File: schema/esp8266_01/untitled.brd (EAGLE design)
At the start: 40.3 x 53.3 mm, 15 parts, among them IC1 LD117AS33TR, X1 22-23-2021

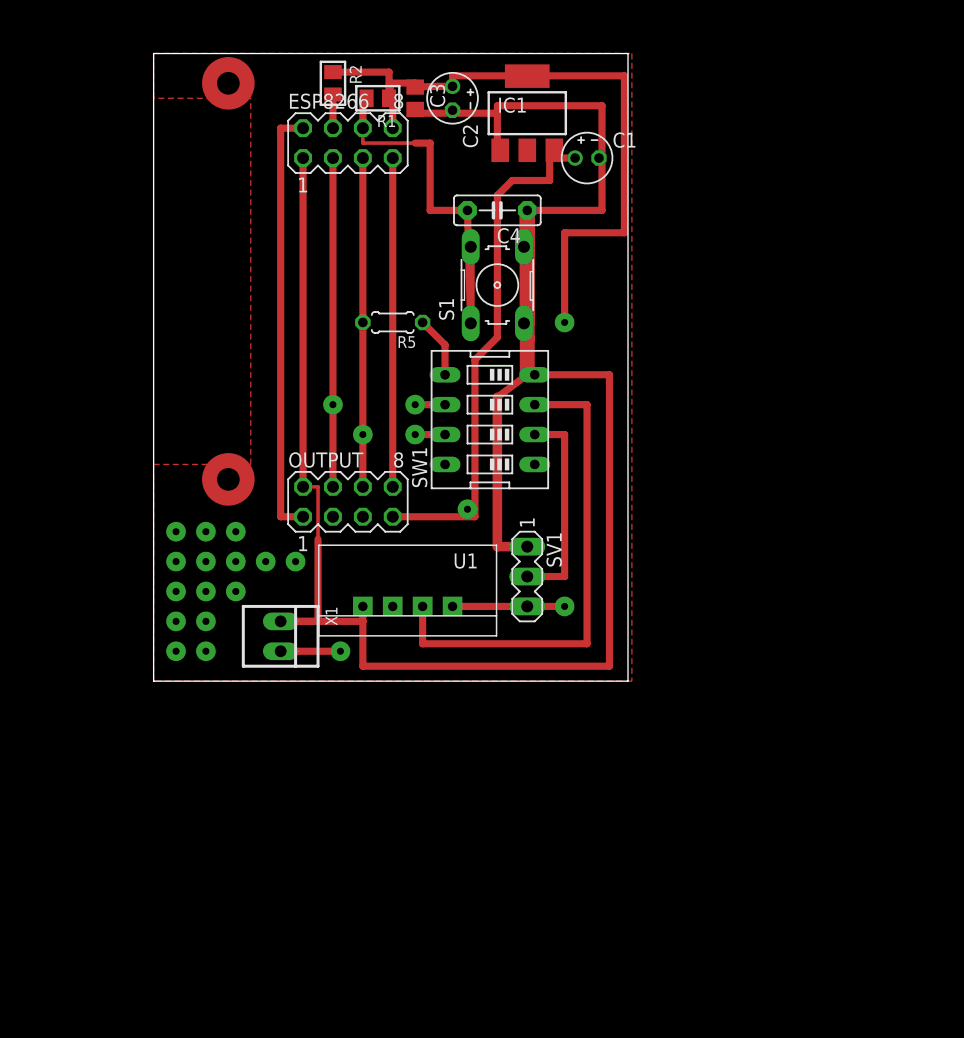
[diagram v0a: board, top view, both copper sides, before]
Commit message: Added ch340
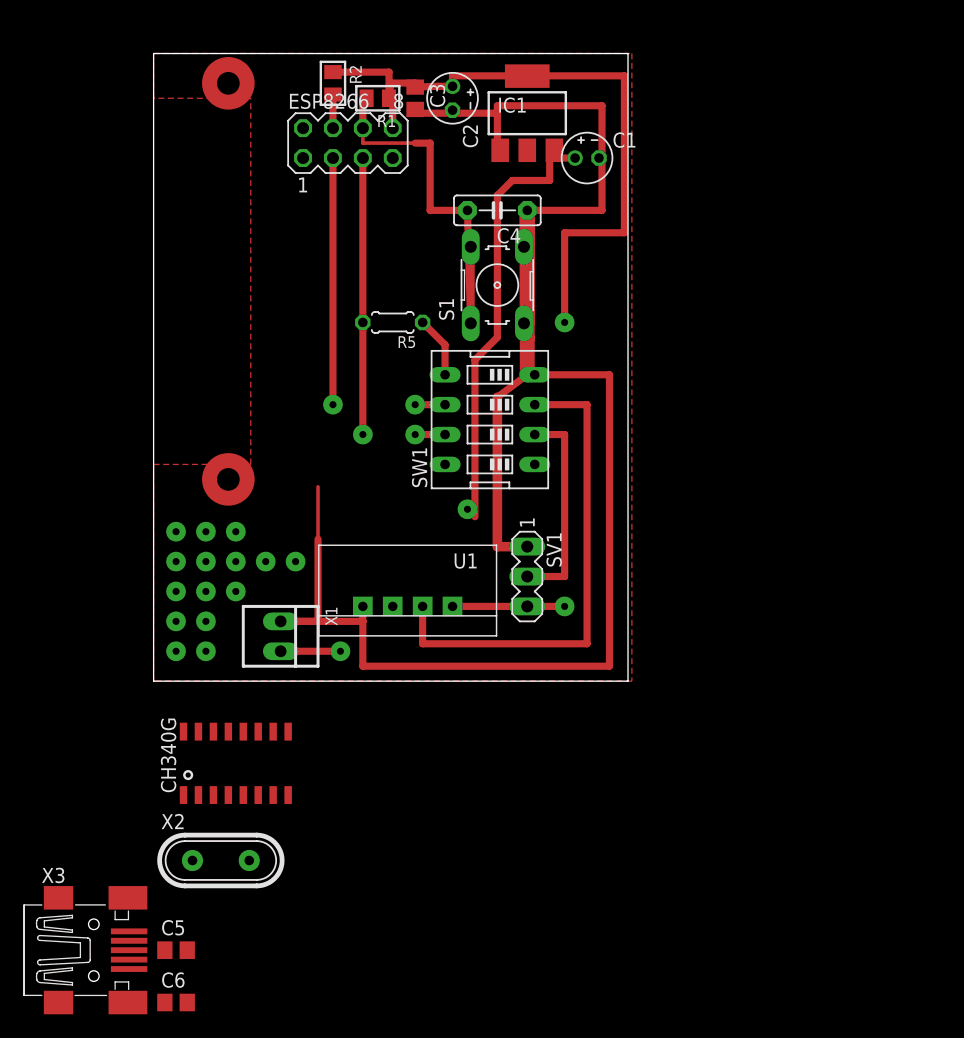
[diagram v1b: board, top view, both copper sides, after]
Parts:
- removed OUTPUT: (no value), con-lstb:MA04-2
- added C5, C6: 22 pF, rcl:C0805
- added U$1: CH340G, usb-serial:SOIC16
- added X2: 12 MHz, IQD-Frequency-Products:HC49
- added X3: MINI-USB-32005-301, con-cypressindustries:32005-301
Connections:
- new net N$27: C5.2, U$1.7, X2.1
- new net N$28: C6.2, U$1.8, X2.2
- net GND: now also C5.1, C6.1; no longer OUTPUT.2
- net GPIO0: no longer OUTPUT.6
- net GPIO2: no longer OUTPUT.4
- net N$11: now also X3.1; no longer OUTPUT.7
- net RX: now also U$1.2; no longer OUTPUT.8
- net TX: now also U$1.3; no longer OUTPUT.1
- net VCC: now also U$1.16
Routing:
- net TX: track 36.8 -> 0.00 mm
- net GND: track 215.7 -> 186.5 mm
- net RX: track 27.9 -> 0.00 mm
- net N$11: track 50.0 -> 43.0 mm
- net GPIO2: track 30.5 -> 23.5 mm
- net GPIO0: track 30.5 -> 26.0 mm
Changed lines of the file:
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@@
 <layers>
 <layer number="1" name="Top" color="4" fill="1" visible="yes" active="yes"/>
-<layer number="16" name="Bottom" color="1" fill="1" visible="no" active="yes"/>
+<layer number="16" name="Bottom" color="1" fill="1" visible="yes" active="yes"/>
 <layer number="17" name="Pads" color="2" fill="1" visible="yes" active="yes"/>
 <layer number="18" name="Vias" color="2" fill="1" visible="yes" active="yes"/>
-<layer number="19" name="Unrouted" color="6" fill="1" visible="no" active="yes"/>
-<layer number="20" name="Dimension" color="15" fill="1" visible="no" active="yes"/>
-<layer number="21" name="tPlace" color="7" fill="1" visible="no" active="yes"/>
-<layer number="22" name="bPlace" color="7" fill="1" visible="no" active="yes"/>
-<layer number="23" name="tOrigins" color="15" fill="1" visible="no" active="yes"/>
-<layer number="24" name="bOrigins" color="15" fill="1" visible="no" active="yes"/>
-<layer number="25" name="tNames" color="7" fill="1" visible="no" active="yes"/>
-<layer number="26" name="bNames" color="7" fill="1" visible="no" active="yes"/>
-<layer number="27" name="tValues" color="7" fill="1" visible="no" active="yes"/>
-<layer number="28" name="bValues" color="7" fill="1" visible="no" active="yes"/>
+<layer number="19" name="Unrouted" color="6" fill="1" visible="yes" active="yes"/>
+<layer number="20" name="Dimension" color="15" fill="1" visible="yes" active="yes"/>
+<layer number="21" name="tPlace" color="7" fill="1" visible="yes" active="yes"/>
+<layer number="22" name="bPlace" color="7" fill="1" visible="yes" active="yes"/>
+<layer number="23" name="tOrigins" color="15" fill="1" visible="yes" active="yes"/>
+<layer number="24" name="bOrigins" color="15" fill="1" visible="yes" active="yes"/>
+<layer number="25" name="tNames" color="7" fill="1" visible="yes" active="yes"/>
+<layer number="26" name="bNames" color="7" fill="1" visible="yes" active="yes"/>
+<layer number="27" name="tValues" color="7" fill="1" visible="yes" active="yes"/>
+<layer number="28" name="bValues" color="7" fill="1" visible="yes" active="yes"/>
 <layer number="29" name="tStop" color="7" fill="3" visible="no" active="yes"/>
 <layer number="30" name="bStop" color="7" fill="6" visible="no" active="yes"/>
@@
 </element>
 <element name="IC1" library="v-reg" package="SOT223" value="LD117AS33TR" x="22.225" y="74.93"/>
-<element name="OUTPUT" library="con-lstb" package="MA04-2" value="" x="6.985" y="41.91">
-<attribute name="OC_NEWARK" value="unknown" x="6.985" y="41.91" size="1.778" layer="27" display="off"/>
-<attribute name="MPN" value="" x="6.985" y="41.91" size="1.778" layer="27" display="off"/>
-<attribute name="MF" value="" x="6.985" y="41.91" size="1.778" layer="27" display="off"/>
-<attribute name="OC_FARNELL" value="unknown" x="6.985" y="41.91" size="1.778" layer="27" display="off"/>
-</element>
 <element name="R1" library="rc-master" package="R0805" value="20K" x="9.525" y="76.2" rot="R180"/>
 <element name="R2" library="rc-master" package="R0805" value="20K" x="5.715" y="77.47" rot="R270"/>
@@
 <attribute name="OC_FARNELL" value="1462926" x="1.27" y="30.48" size="1.778" layer="27" rot="R270" display="off"/>
 </element>
+<element name="U$1" library="usb-serial" package="SOIC16" value="CH340G" x="-2.54" y="19.685"/>
+<element name="X2" library="IQD-Frequency-Products" package="HC49" value="12 MHz" x="-3.81" y="11.43"/>
+<element name="C5" library="rcl" package="C0805" value="22 pF" x="-7.62" y="3.81"/>
+<element name="C6" library="rcl" package="C0805" value="22 pF" x="-7.62" y="-0.635"/>
+<element name="X3" library="con-cypressindustries" package="32005-301" value="MINI-USB-32005-301" x="-14.605" y="3.81">
+<attribute name="OC_NEWARK" value="unknown" x="-14.605" y="3.81" size="1.778" layer="27" display="off"/>
+<attribute name="MPN" value="" x="-14.605" y="3.81" size="1.778" layer="27" display="off"/>
+<attribute name="MF" value="" x="-14.605" y="3.81" size="1.778" layer="27" display="off"/>
+<attribute name="OC_FARNELL" value="unknown" x="-14.605" y="3.81" size="1.778" layer="27" display="off"/>
+</element>
 </elements>
 <signals>
@@
 <contactref element="S1" pad="3"/>
 <contactref element="C3" pad="2"/>
-<contactref element="OUTPUT" pad="2"/>
-<wire x1="3.175" y1="43.18" x2="4.445" y2="43.18" width="0.3048" layer="1"/>
 <wire x1="8.255" y1="27.94" x2="29.21" y2="27.94" width="0.6096" layer="1"/>
 <wire x1="22.86" y1="52.705" x2="22.225" y2="52.705" width="1.27" layer="1"/>
@@
 <contactref element="SV1" pad="1"/>
 <wire x1="8.255" y1="31.75" x2="8.255" y2="27.94" width="0.6096" layer="1"/>
-<wire x1="3.175" y1="71.12" x2="3.175" y2="43.18" width="0.6096" layer="1"/>
 <wire x1="12.7" y1="75.25" x2="12.7" y2="74.93" width="0.6096" layer="1"/>
 <wire x1="12.7" y1="74.93" x2="15.875" y2="74.93" width="0.6096" layer="1"/>
@@
 <wire x1="1.27" y1="31.75" x2="4.445" y2="31.75" width="0.6096" layer="1"/>
 <wire x1="4.445" y1="31.75" x2="4.445" y2="38.735" width="0.6096" layer="1"/>
+<contactref element="C6" pad="1"/>
+<contactref element="C5" pad="1"/>
+<wire x1="12.7" y1="74.93" x2="3.175" y2="71.12" width="0" layer="19" extent="1-1"/>
+<wire x1="-8.57" y1="3.81" x2="8.255" y2="27.94" width="0" layer="19" extent="1-1"/>
+<wire x1="-8.57" y1="-0.635" x2="-8.57" y2="3.81" width="0" layer="19" extent="1-1"/>
 </signal>
 <signal name="VCC">
@@
 <via x="25.4" y="33.02" extent="1-16" drill="0.6" diameter="1.6764" shape="square"/>
 <wire x1="22.225" y1="33.02" x2="25.4" y2="33.02" width="0.6096" layer="1"/>
+<contactref element="U$1" pad="16"/>
 <wire x1="15.875" y1="33.02" x2="10.795" y2="73.66" width="0" layer="19" extent="1-1"/>
+<wire x1="-6.985" y1="22.38" x2="15.875" y2="33.02" width="0" layer="19" extent="1-1"/>
 </signal>
 <signal name="RESET">
@@
 <signal name="GPIO2">
 <contactref element="ESP8266" pad="3"/>
-<contactref element="OUTPUT" pad="4"/>
 <contactref element="SW1" pad="6"/>
 <wire x1="5.715" y1="50.165" x2="5.715" y2="71.12" width="0.6096" layer="1"/>
 <via x="5.715" y="50.165" extent="1-16" drill="0.6" diameter="1.6764" shape="square"/>
-<wire x1="5.715" y1="43.18" x2="5.715" y2="50.165" width="0.6096" layer="1"/>
 <wire x1="15.24" y1="50.165" x2="12.7" y2="50.165" width="0.6096" layer="1"/>
 <wire x1="5.715" y1="50.165" x2="12.7" y2="50.165" width="0" layer="19" extent="1-1"/>
@@
 <signal name="GPIO0">
 <contactref element="ESP8266" pad="5"/>
-<contactref element="OUTPUT" pad="6"/>
 <contactref element="R5" pad="2"/>
 <wire x1="8.255" y1="57.15" x2="8.255" y2="47.625" width="0.6096" layer="1"/>
@@
 <contactref element="SW1" pad="7"/>
 <via x="8.255" y="47.625" extent="1-16" drill="0.6" diameter="1.6764" shape="square"/>
-<wire x1="8.255" y1="43.18" x2="8.255" y2="47.625" width="0.6096" layer="1"/>
 <wire x1="15.24" y1="47.625" x2="12.7" y2="47.625" width="0.6096" layer="1"/>
 <wire x1="8.255" y1="47.625" x2="12.7" y2="47.625" width="0" layer="19" extent="1-1"/>
-</signal>
-<signal name="RX">
-<contactref element="ESP8266" pad="7"/>
-<contactref element="OUTPUT" pad="8"/>
-<wire x1="10.795" y1="71.12" x2="10.795" y2="43.18" width="0.6096" layer="1"/>
-</signal>
-<signal name="TX">
-<contactref element="ESP8266" pad="2"/>
-<contactref element="OUTPUT" pad="1"/>
-<wire x1="3.175" y1="73.66" x2="1.27" y2="73.66" width="0.6096" layer="1"/>
-<wire x1="1.27" y1="73.66" x2="1.27" y2="40.64" width="0.6096" layer="1"/>
-<wire x1="1.27" y1="40.64" x2="3.175" y2="40.64" width="0.6096" layer="1"/>
 </signal>
 <signal name="N$2">
@@
 <contactref element="X1" pad="2"/>
 <contactref element="C1" pad="+"/>
-<contactref element="OUTPUT" pad="7"/>
 <contactref element="IC1" pad="3"/>
-<wire x1="10.795" y1="40.64" x2="17.78" y2="40.64" width="0.6096" layer="1"/>
 <wire x1="17.78" y1="40.64" x2="17.78" y2="53.975" width="0.6096" layer="1"/>
 <wire x1="17.78" y1="53.975" x2="19.685" y2="55.88" width="0.6096" layer="1"/>
@@
 <via x="6.35" y="29.21" extent="1-16" drill="0.6" diameter="1.6764" shape="square"/>
 <wire x1="1.27" y1="29.21" x2="6.35" y2="29.21" width="0.6096" layer="1"/>
-<wire x1="6.35" y1="29.21" x2="10.795" y2="40.64" width="0" layer="19" extent="1-1"/>
+<contactref element="X3" pad="1"/>
+<wire x1="6.35" y1="29.21" x2="17.78" y2="40.64" width="0" layer="19" extent="1-1"/>
+<wire x1="-11.605" y1="5.41" x2="1.27" y2="29.21" width="0" layer="19" extent="1-1"/>
 </signal>
 <signal name="N$15">
@@
 <via x="-5.08" y="29.21" extent="1-16" drill="0.6" diameter="1.6764" shape="square"/>
 </signal>
+<signal name="N$27">
+<contactref element="U$1" pad="7"/>
+<contactref element="X2" pad="1"/>
+<contactref element="C5" pad="2"/>
+<wire x1="-6.223" y1="11.43" x2="0.635" y2="16.99" width="0" layer="19" extent="1-1"/>
+<wire x1="-6.67" y1="3.81" x2="-6.223" y2="11.43" width="0" layer="19" extent="1-1"/>
+</signal>
+<signal name="N$28">
+<contactref element="U$1" pad="8"/>
+<contactref element="X2" pad="2"/>
+<contactref element="C6" pad="2"/>
+<wire x1="-1.397" y1="11.43" x2="1.905" y2="16.99" width="0" layer="19" extent="1-1"/>
+<wire x1="-6.67" y1="-0.635" x2="-1.397" y2="11.43" width="0" layer="19" extent="1-1"/>
+</signal>
+<signal name="RX">
+<contactref element="ESP8266" pad="7"/>
+<contactref element="U$1" pad="2"/>
+<wire x1="-5.715" y1="16.99" x2="10.795" y2="71.12" width="0" layer="19" extent="1-1"/>
+</signal>
+<signal name="TX">
+<contactref element="U$1" pad="3"/>
+<contactref element="ESP8266" pad="2"/>
+<wire x1="-4.445" y1="16.99" x2="3.175" y2="73.66" width="0" layer="19" extent="1-1"/>
+</signal>
 </signals>

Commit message: Added normal dht22 lib. Fixed known issues. looks like stable
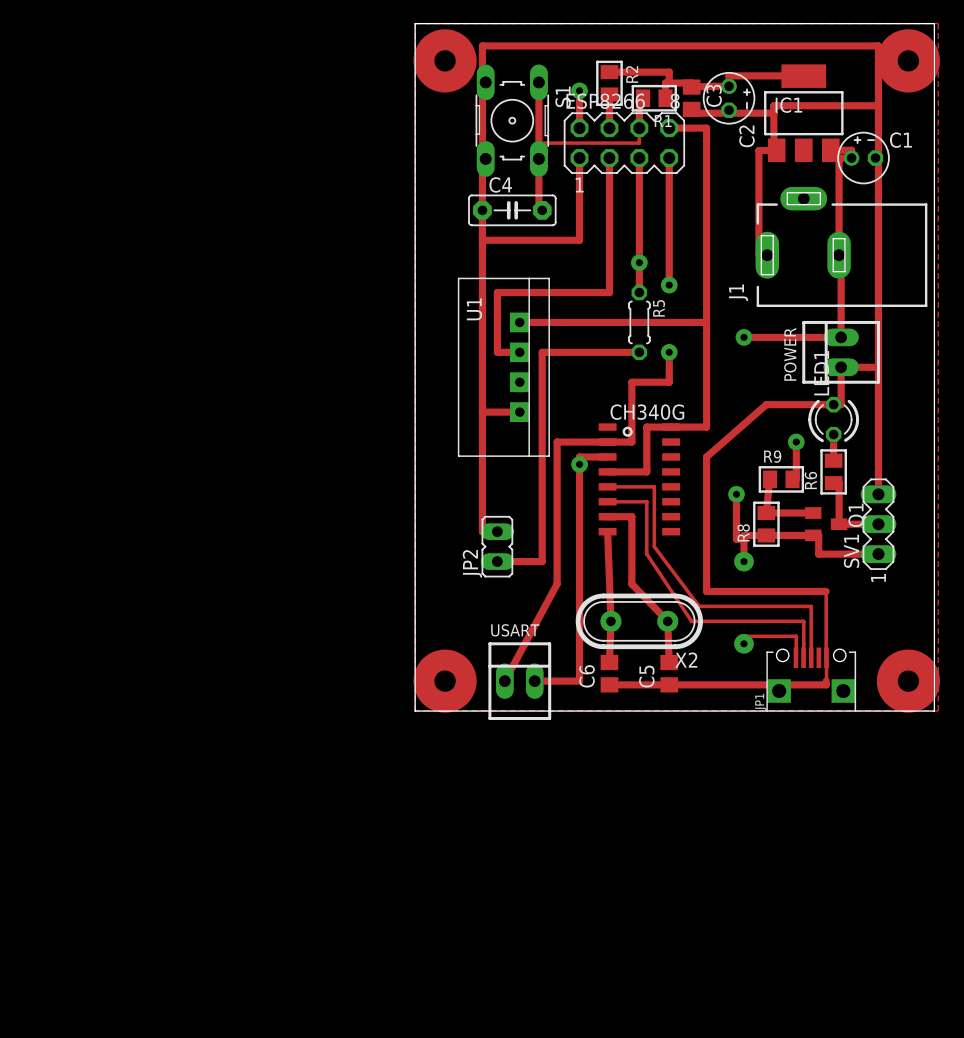
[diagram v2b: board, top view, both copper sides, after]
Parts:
- removed SW1: (no value), special:EDG-04
- removed X1: 22-23-2021, con-molex:22-23-2021
- removed X3: MINI-USB-32005-301, con-cypressindustries:32005-301
- added J1: DCJ0202, con-jack:DCJ0202
- added JP1: USB-RECEPTABLE, daspilker:FCI-10103594-0001LF
- added JP2: (no value), jumper:JP1
- added LED1: (no value), led:LED3MM
- added POWER, USART: 22-23-2021, con-molex:22-23-2021
- added Q1: BC857ASMD, transistor-pnp:SOT23-BEC
- added R6, R8: 1K, rc-master:R0805
- added R9: 4.7K, rc-master:R0805
- moved C5 48.0 mm to (34.3, 27.3), turned to 90 degrees
- moved C6 46.2 mm to (29.2, 27.3), turned to 90 degrees
- moved U$1 41.9 mm to (31.8, 43.8), turned to 270 degrees
- moved X2 41.0 mm to (31.8, 31.8), turned to 180 degrees
- moved SV1 30.2 mm to (52.1, 40.0), turned to 90 degrees
- moved R1 23.5 mm to (33.0, 76.2)
- moved C3 23.5 mm to (36.2, 76.2)
- moved ESP8266 23.5 mm to (30.5, 72.4)
- moved R2 23.5 mm to (29.2, 77.5)
- moved C1 23.5 mm to (50.8, 71.1)
- moved C2 23.5 mm to (39.4, 76.2)
- moved IC1 23.5 mm to (45.7, 74.9)
- moved U1 22.4 mm to (21.6, 53.3), turned to 270 degrees
- moved R5 21.0 mm to (31.8, 57.1), turned to 270 degrees
- moved S1 14.0 mm to (21.0, 74.3), turned to 270 degrees
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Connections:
- removed net N$11: C1.+, IC1.3, X1.2, X3.1
- new net N$29: JP1.2, U$1.6
- new net N$31: JP1.3, U$1.5
- new net N$32: LED1.A, R6.2
- new net N$37: C1.+, IC1.3, J1.3, JP1.1, POWER.2, Q1.E, R8.1, SV1.1
- net GND: now also J1.1, JP1.5, JP2.2, LED1.K, POWER.1, SV1.3; no longer SV1.1, SW1.4, X1.1
- net GPIO0: now also R5.1, R9.2; no longer R5.2, SW1.7
- net GPIO2: now also U1.DATA; no longer SW1.6
- net N$1: now also JP2.1, R5.2; no longer R5.1, SW1.5
- net N$3: now also Q1.B, R8.2, R9.1; no longer SW1.3, U1.DATA
- net N$7: now also Q1.C, R6.1; no longer SW1.2
- net RX: now also ESP8266.2, U$1.3, USART.2; no longer ESP8266.7, U$1.2
- net TX: now also ESP8266.7, U$1.2, USART.1; no longer ESP8266.2, U$1.3
- net VCC: now also U$1.4; no longer SV1.3
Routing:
- net N$37: track 0.00 -> 53.8 mm, vias 0 -> 4
- net TX: track 0.00 -> 49.4 mm, vias 0 -> 2
- net GND: track 186.5 -> 232.6 mm
- net VCC: track 33.5 -> 77.0 mm, vias 1 -> 0
- net N$11: track 43.0 -> 0.00 mm, vias 1 -> 0
- net N$3: track 41.9 -> 7.49 mm
- net N$17: track 33.7 -> 0.00 mm, vias 1 -> 0
- net N$31: track 0.00 -> 29.3 mm
- net RX: track 0.00 -> 28.4 mm, vias 0 -> 2
- net N$29: track 0.00 -> 27.3 mm
- net N$1: track 5.23 -> 29.8 mm
- net RESET: track 42.5 -> 25.1 mm
- net N$27: track 0.00 -> 15.7 mm
- net N$28: track 0.00 -> 11.1 mm
- net GPIO0: track 26.0 -> 14.9 mm
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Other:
- board size 40.3 x 53.3 mm -> 44.1 x 58.4 mm
